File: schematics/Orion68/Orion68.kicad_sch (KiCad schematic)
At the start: 0 parts

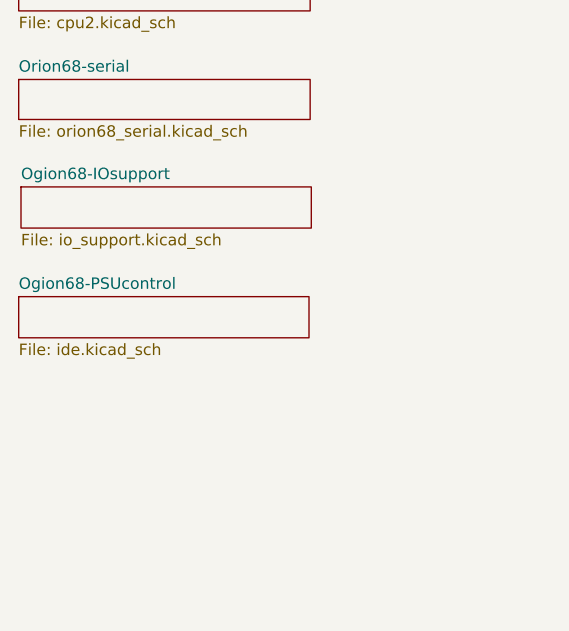
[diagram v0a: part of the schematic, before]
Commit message: 2026-09-15: added picoIDE
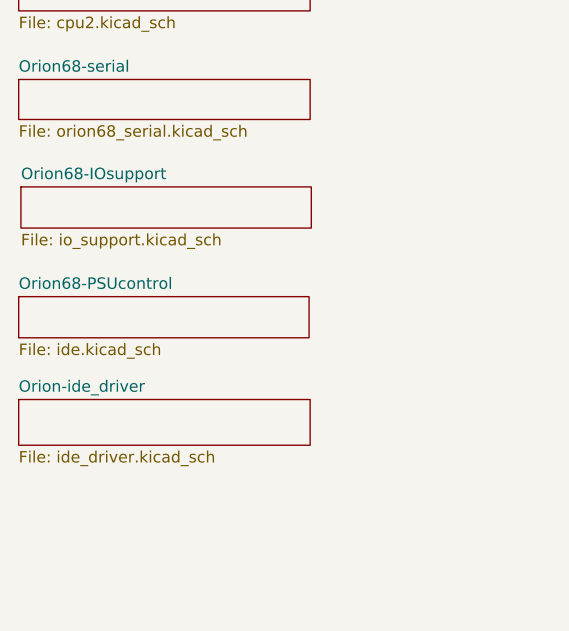
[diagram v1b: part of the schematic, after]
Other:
- sheet Ogion68-IOsupport renamed Orion68-IOsupport
- sheet Ogion68-PSUcontrol renamed Orion68-PSUcontrol
- added sheet Orion-ide_driver (ide_driver.kicad_sch)
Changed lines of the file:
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@@
 			(color 0 0 0 0.0000)
 		)
-		(property "Sheetname" "Ogion68-IOsupport"
+		(property "Sheetname" "Orion68-IOsupport"
 			(at 19.304 102.6664 0)
 			(effects
@@
 	)
 	(sheet
+		(at 19.05 127)
+		(size 32.385 5.08)
+		(exclude_from_sim no)
+		(in_bom yes)
+		(on_board yes)
+		(dnp no)
+		(fields_autoplaced yes)
+		(stroke
+			(width 0.1524)
+			(type solid)
+		)
+		(fill
+			(color 0 0 0 0.0000)
+		)
+		(property "Sheetname" "Orion-ide_driver"
+			(at 19.05 126.2884 0)
+			(effects
+				(font
+					(size 1.27 1.27)
+				)
+				(justify left bottom)
+			)
+		)
+		(property "Sheetfile" "ide_driver.kicad_sch"
+			(at 19.05 132.6646 0)
+			(effects
+				(font
+					(size 1.27 1.27)
+				)
+				(justify left top)
+			)
+		)
+		(instances
+			(project "Orion68"
+				(path "/c7ab032b-c937-44de-ab42-c91dee57f0a8"
+					(page "10")
+				)
+			)
+		)
+	)
+	(sheet
 		(at 19.05 115.57)
 		(size 32.258 4.572)
@@
 			(color 0 0 0 0.0000)
 		)
-		(property "Sheetname" "Ogion68-PSUcontrol"
+		(property "Sheetname" "Orion68-PSUcontrol"
 			(at 19.05 114.8584 0)
 			(effects
